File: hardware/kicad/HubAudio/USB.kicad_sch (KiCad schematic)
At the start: 6 parts, among them J2 USB_C_Receptacle_USB2.0_16P

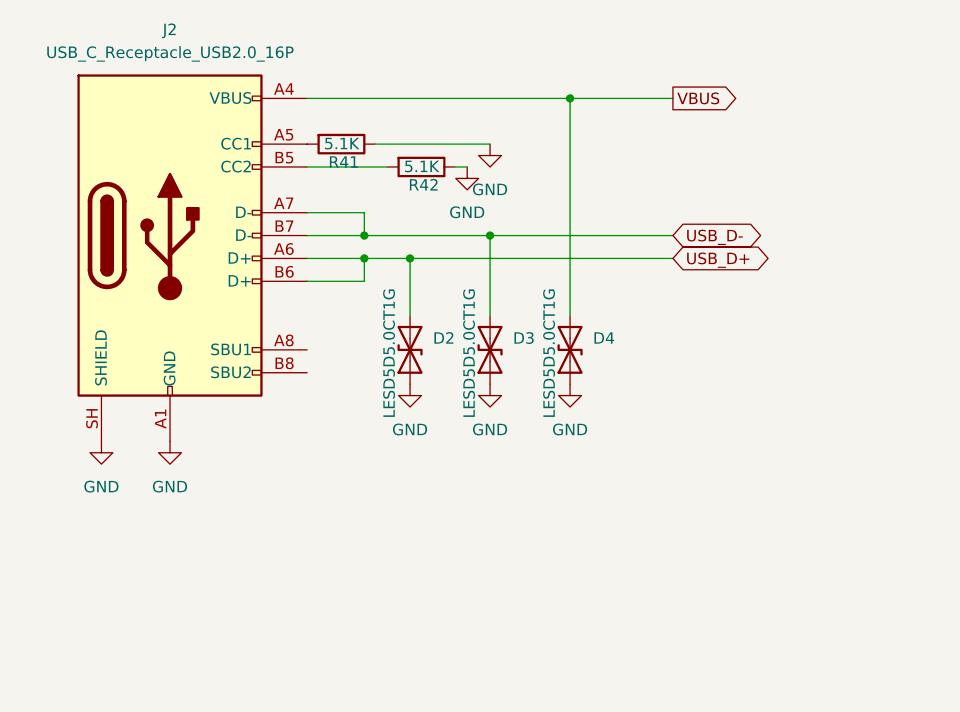
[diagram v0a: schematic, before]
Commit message: Finalize I2C and SPI control architecture
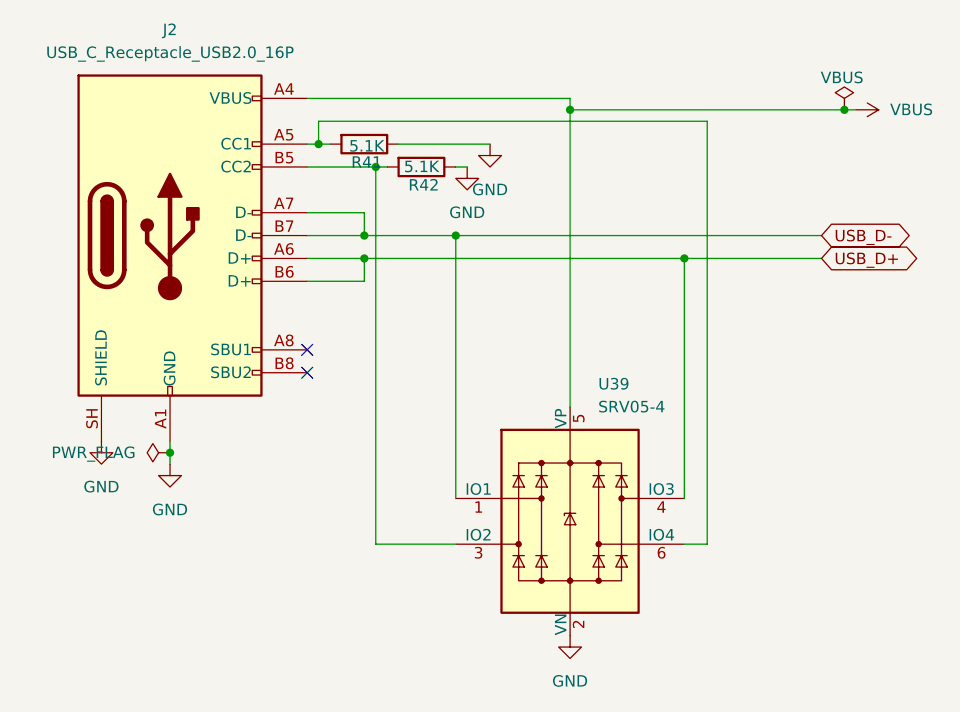
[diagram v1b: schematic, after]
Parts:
- removed D2, D3, D4: LESD5D5.0CT1G, Diode_SMD:D_SOD-523, symbol Device:D_TVS
- added U39: SRV05-4, Package_TO_SOT_SMD:SOT-23-6, symbol Power_Protection:SRV05-4
- R41, R42: PNM (none) -> RC0805FR-075K1L
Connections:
- net GND: now also U39.2 (VN)
- net USB_D+: now also U39.4 (IO3)
- net USB_D-: now also U39.1 (IO1)
- net VBUS: now also U39.5 (VP)
- net at J2.B5 (CC2), R42.2: now also U39.3 (IO2)
- net at J2.A5 (CC1), R41.2: now also U39.6 (IO4)
- no-connect marks 0 -> 2
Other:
- moved on the sheet: R41
